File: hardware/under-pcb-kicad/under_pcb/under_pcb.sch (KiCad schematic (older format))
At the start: 15 parts, among them J1 Conn_01x08, J10 Conn_01x01, J11 Conn_01x01, J2 Conn_01x08, J3 Conn_01x08, J4 Conn_01x06, J5 Conn_02x18_Odd_Even, J6 Conn_01x08, J7 Conn_01x04, J8 Conn_01x03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

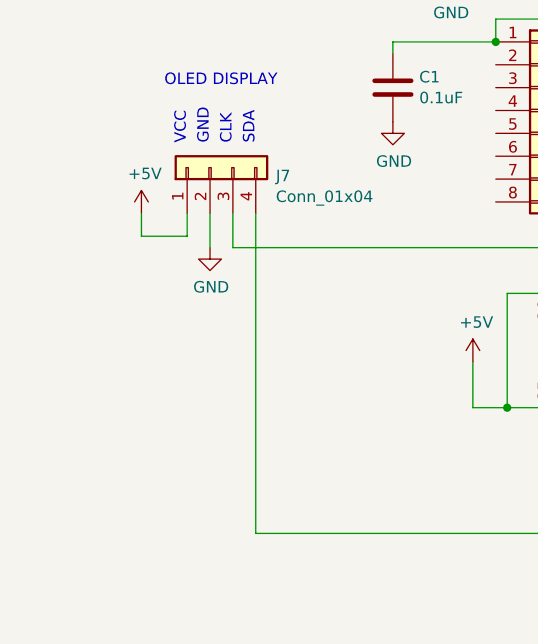
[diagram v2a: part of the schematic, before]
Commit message: add supply jumper on OLED for patty board
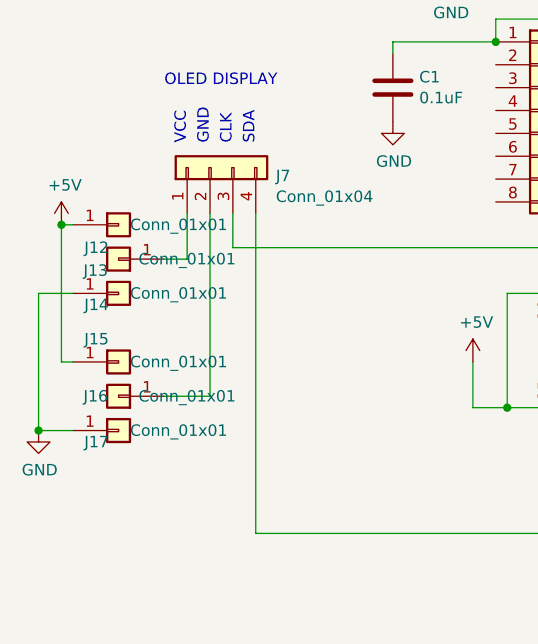
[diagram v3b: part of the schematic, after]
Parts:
- added J12, J13, J14, J15, J16, J17: Conn_01x01, Connector_PinSocket_2.54mm:PinSocket_1x01_P2.54mm_Vertical, symbol Connector_Generic:Conn_01x01
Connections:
- net +5V: now also J12.1 (Pin_1), J15.1 (Pin_1); no longer J7.1 (Pin_1)
- net GND: now also J14.1 (Pin_1), J17.1 (Pin_1); no longer J7.2 (Pin_2)
- new net: J13.1 (Pin_1), J7.1 (Pin_1)
- new net: J16.1 (Pin_1), J7.2 (Pin_2)
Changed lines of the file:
@@
 L power:+5V #PWR0105
 U 1 1 5E4D34BE
-P 2650 4300
-F 0 "#PWR0105" H 2650 4150 50  0001 C CNN
-F 1 "+5V" H 2665 4473 50  0000 C CNN
-F 2 "" H 2650 4300 50  0001 C CNN
-F 3 "" H 2650 4300 50  0001 C CNN
-	1    2650 4300
-	1    0    0    -1
-$EndComp
-Wire Wire Line
-	2850 4300 2850 4400
-Wire Wire Line
-	2850 4400 2650 4400
-Wire Wire Line
-	2650 4400 2650 4300
+P 2300 4350
+F 0 "#PWR0105" H 2300 4200 50  0001 C CNN
+F 1 "+5V" H 2315 4523 50  0000 C CNN
+F 2 "" H 2300 4350 50  0001 C CNN
+F 3 "" H 2300 4350 50  0001 C CNN
+	1    2300 4350
+	1    0    0    -1
+$EndComp
 $Comp
 L power:GND #PWR0106
@@
 L power:GND #PWR0109
 U 1 1 5E50711A
-P 2950 4450
-F 0 "#PWR0109" H 2950 4200 50  0001 C CNN
-F 1 "GND" H 2955 4277 50  0000 C CNN
-F 2 "" H 2950 4450 50  0001 C CNN
-F 3 "" H 2950 4450 50  0001 C CNN
-	1    2950 4450
-	1    0    0    -1
-$EndComp
-Wire Wire Line
-	2950 4300 2950 4450
+P 2200 5250
+F 0 "#PWR0109" H 2200 5000 50  0001 C CNN
+F 1 "GND" H 2205 5077 50  0000 C CNN
+F 2 "" H 2200 5250 50  0001 C CNN
+F 3 "" H 2200 5250 50  0001 C CNN
+	1    2200 5250
+	1    0    0    -1
+$EndComp
 $Comp
 L Connector_Generic:Conn_02x18_Odd_Even J5
@@
 	1    0    0    -1
 $EndComp
+$Comp
+L Connector_Generic:Conn_01x01 J13
+U 1 1 5E5B7EFF
+P 2550 4500
+F 0 "J13" H 2650 4550 50  0000 C CNN
+F 1 "Conn_01x01" H 2250 4500 50  0000 C CNN
+F 2 "Connector_PinSocket_2.54mm:PinSocket_1x01_P2.54mm_Vertical" H 2550 4500 50  0001 C CNN
+F 3 "~" H 2550 4500 50  0001 C CNN
+	1    2550 4500
+	-1   0    0    1
+$EndComp
+$Comp
+L Connector_Generic:Conn_01x01 J16
+U 1 1 5E5B8616
+P 2550 5100
+F 0 "J16" H 2650 5100 50  0000 C CNN
+F 1 "Conn_01x01" H 2250 5100 50  0000 C CNN
+F 2 "Connector_PinSocket_2.54mm:PinSocket_1x01_P2.54mm_Vertical" H 2550 5100 50  0001 C CNN
+F 3 "~" H 2550 5100 50  0001 C CNN
+	1    2550 5100
+	-1   0    0    1
+$EndComp
+$Comp
+L Connector_Generic:Conn_01x01 J12
+U 1 1 5E5B8D9E
+P 2550 4350
+F 0 "J12" H 2400 4250 50  0000 L CNN
+F 1 "Conn_01x01" H 2600 4350 50  0000 L CNN
+F 2 "Connector_PinSocket_2.54mm:PinSocket_1x01_P2.54mm_Vertical" H 2550 4350 50  0001 C CNN
+F 3 "~" H 2550 4350 50  0001 C CNN
+	1    2550 4350
+	1    0    0    -1
+$EndComp
+$Comp
+L Connector_Generic:Conn_01x01 J14
+U 1 1 5E5B98BC
+P 2550 4650
+F 0 "J14" H 2400 4600 50  0000 L CNN
+F 1 "Conn_01x01" H 2600 4650 50  0000 L CNN
+F 2 "Connector_PinSocket_2.54mm:PinSocket_1x01_P2.54mm_Vertical" H 2550 4650 50  0001 C CNN
+F 3 "~" H 2550 4650 50  0001 C CNN
+	1    2550 4650
+	1    0    0    -1
+$EndComp
+Wire Wire Line
+	2750 4500 2850 4500
+Wire Wire Line
+	2850 4500 2850 4300
+Wire Wire Line
+	2950 5100 2950 4300
+Wire Wire Line
+	2750 5100 2950 5100
+$Comp
+L Connector_Generic:Conn_01x01 J15
+U 1 1 5E5C5E3D
+P 2550 4950
+F 0 "J15" H 2400 5050 50  0000 L CNN
+F 1 "Conn_01x01" H 2600 4950 50  0000 L CNN
+F 2 "Connector_PinSocket_2.54mm:PinSocket_1x01_P2.54mm_Vertical" H 2550 4950 50  0001 C CNN
+F 3 "~" H 2550 4950 50  0001 C CNN
+	1    2550 4950
+	1    0    0    -1
+$EndComp
+$Comp
+L Connector_Generic:Conn_01x01 J17
+U 1 1 5E5C5EDD
+P 2550 5250
+F 0 "J17" H 2400 5200 50  0000 L CNN
+F 1 "Conn_01x01" H 2600 5250 50  0000 L CNN
+F 2 "Connector_PinSocket_2.54mm:PinSocket_1x01_P2.54mm_Vertical" H 2550 5250 50  0001 C CNN
+F 3 "~" H 2550 5250 50  0001 C CNN
+	1    2550 5250
+	1    0    0    -1
+$EndComp
+Wire Wire Line
+	2350 4950 2300 4950
+Wire Wire Line
+	2300 4950 2300 4350
+Wire Wire Line
+	2350 4350 2300 4350
+Connection ~ 2300 4350
+Wire Wire Line
+	2350 4650 2200 4650
+Wire Wire Line
+	2200 4650 2200 5250
+Wire Wire Line
+	2350 5250 2200 5250
+Connection ~ 2200 5250
 $EndSCHEMATC
